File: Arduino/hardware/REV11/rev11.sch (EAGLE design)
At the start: 30 parts, among them IC2 ATMEGA168-AU, Q1 32768Hz

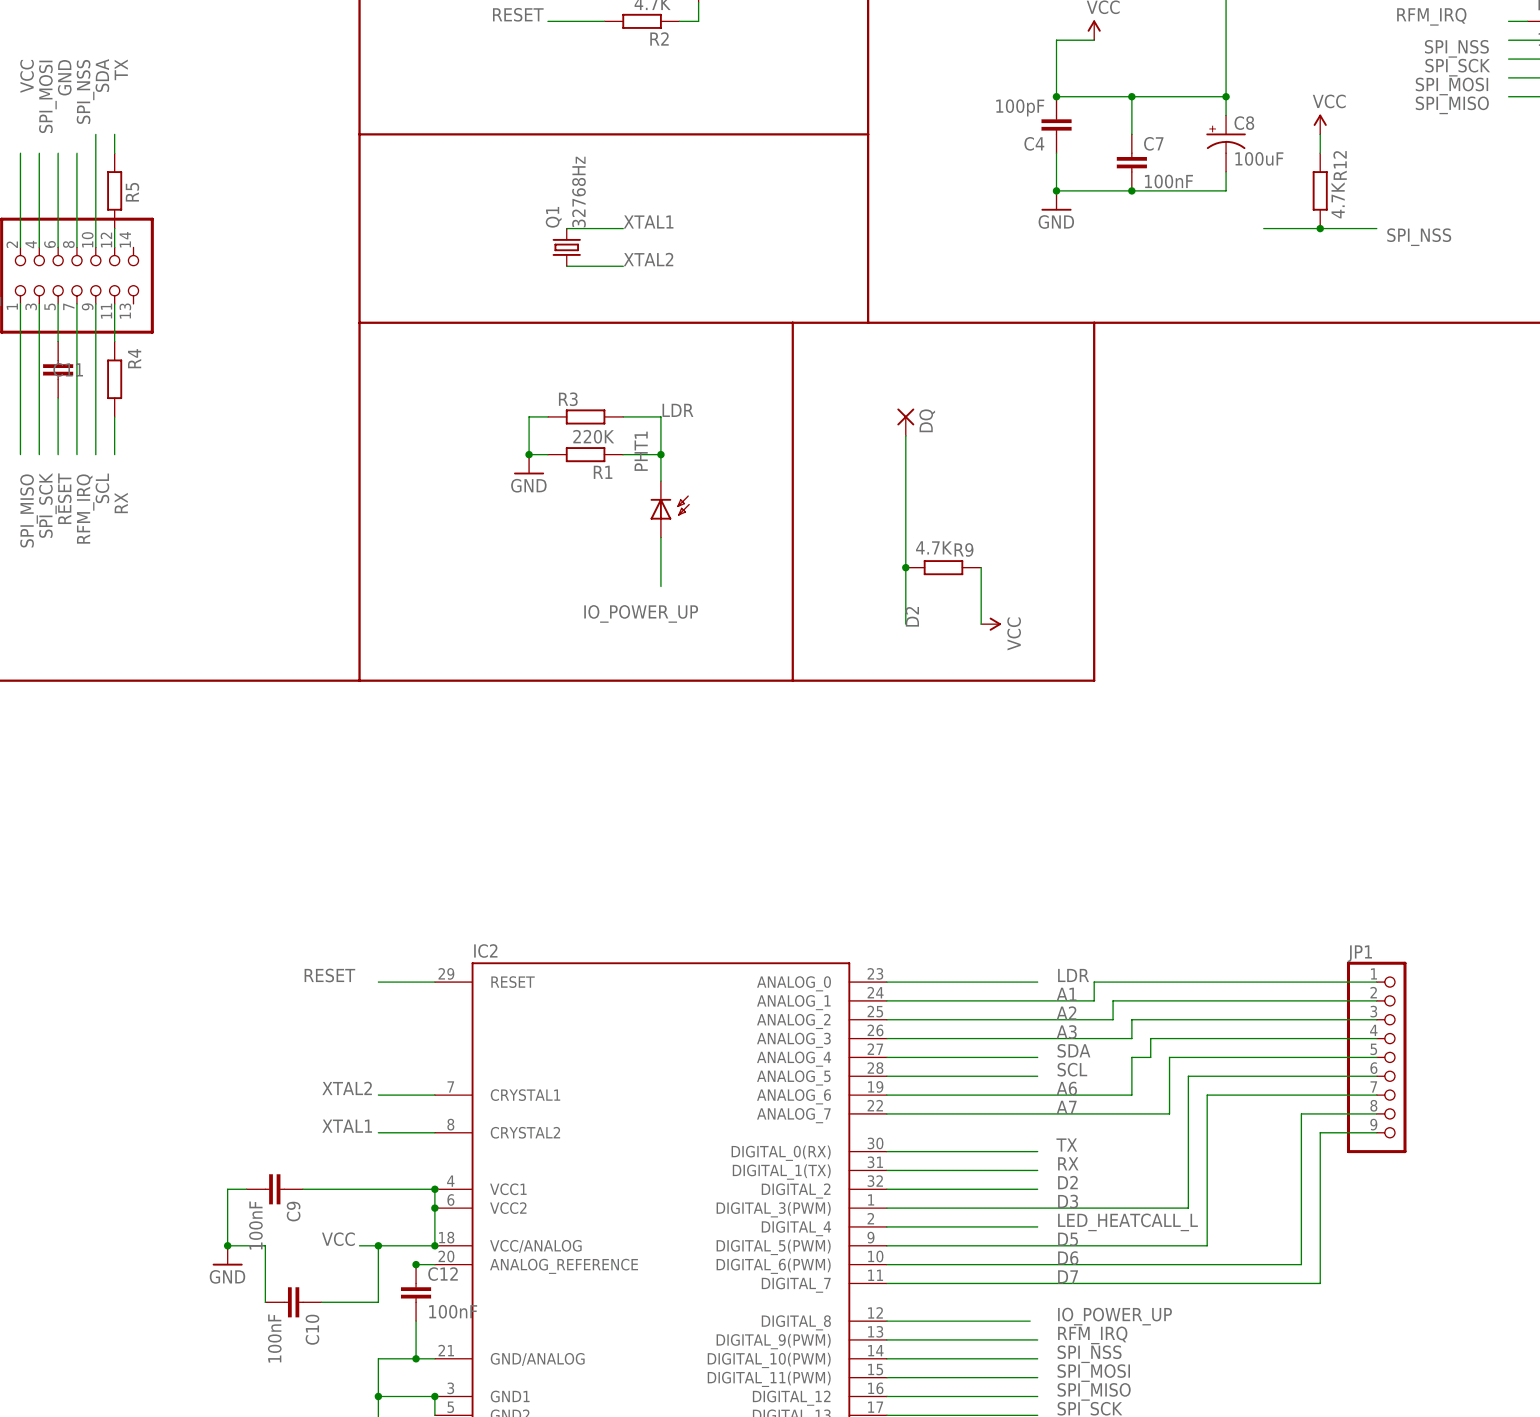
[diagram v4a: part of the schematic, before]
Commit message: moved DQ/D2 to gpio connector and I2C ext
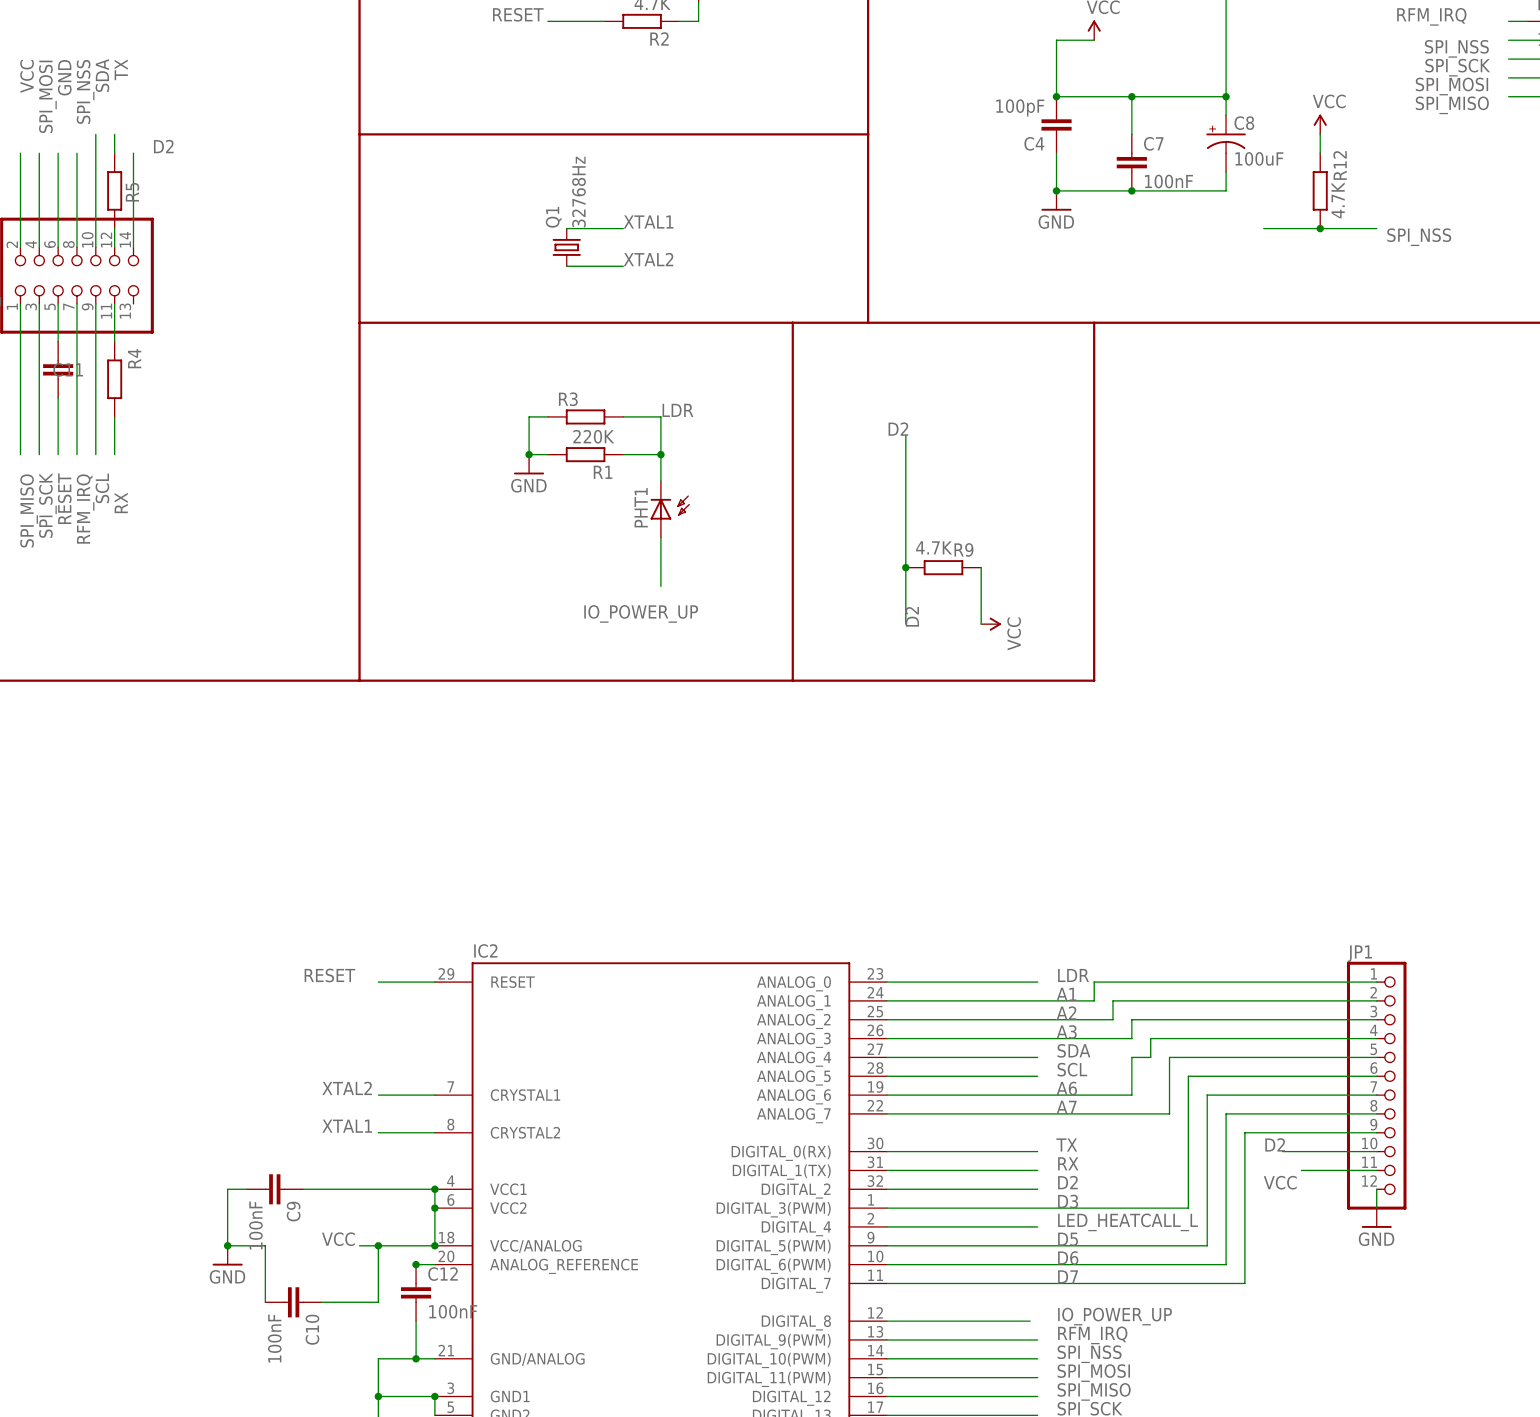
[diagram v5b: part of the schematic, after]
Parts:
- removed DQ: (no value), wirepad:2,15/1,0
- JP1: device pinhead:PINHD-1X9 -> pinhead:PINHD-1X12
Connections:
- net D2: now also JP1.10; no longer DQ.P
- net GND: now also JP1.12
- net VCC: now also JP1.11
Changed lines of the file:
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@@
 <part name="R9" library="resistor" deviceset="R-EU_" device="R0603" value="4.7K"/>
 <part name="P+1" library="SparkFun-Aesthetics" deviceset="VCC" device=""/>
-<part name="DQ" library="wirepad" deviceset="2,15/1,0" device=""/>
-<part name="JP1" library="pinhead" deviceset="PINHD-1X9" device=""/>
+<part name="JP1" library="pinhead" deviceset="PINHD-1X12" device=""/>
 <part name="PHT1" library="opto-trans-siemens" deviceset="BPX65" device=""/>
+<part name="GND2" library="SparkFun-Aesthetics" deviceset="GND" device=""/>
 </parts>
 <sheets>
@@
 </instance>
 <instance part="P+1" gate="G$1" x="241.3" y="167.64" rot="R270"/>
-<instance part="DQ" gate="1" x="231.14" y="195.58" rot="R270"/>
-<instance part="JP1" gate="A" x="297.18" y="109.22"/>
+<instance part="JP1" gate="G$1" x="297.18" y="106.68"/>
 <instance part="PHT1" gate="1" x="198.12" y="181.864" smashed="yes" rot="R180">
-<attribute name="NAME" x="194.564" y="193.802" size="1.778" layer="95" rot="R270"/>
-</instance>
+<attribute name="NAME" x="194.564" y="186.182" size="1.778" layer="95" rot="R270"/>
+</instance>
+<instance part="GND2" gate="1" x="294.64" y="86.36"/>
 </instances>
 <busses>
@@
 <wire x1="241.3" y1="167.64" x2="241.3" y2="175.26" width="0.1524" layer="91"/>
 </segment>
+<segment>
+<wire x1="294.64" y1="93.98" x2="284.48" y2="93.98" width="0.1524" layer="91"/>
+<label x="279.4" y="91.44" size="1.778" layer="95"/>
+<pinref part="JP1" gate="G$1" pin="11"/>
+</segment>
 </net>
 <net name="GND" class="1">
@@
 <junction x="180.34" y="190.5"/>
 </segment>
+<segment>
+<pinref part="JP1" gate="G$1" pin="12"/>
+<pinref part="GND2" gate="1" pin="GND"/>
+<wire x1="294.64" y1="88.9" x2="294.64" y2="91.44" width="0.1524" layer="91"/>
+</segment>
 </net>
 <net name="D6" class="0">
 <segment>
-<wire x1="228.6" y1="81.28" x2="284.48" y2="81.28" width="0.1524" layer="91"/>
-<wire x1="284.48" y1="81.28" x2="284.48" y2="101.6" width="0.1524" layer="91"/>
-<wire x1="284.48" y1="101.6" x2="294.64" y2="101.6" width="0.1524" layer="91"/>
+<wire x1="228.6" y1="81.28" x2="274.32" y2="81.28" width="0.1524" layer="91"/>
+<wire x1="274.32" y1="81.28" x2="274.32" y2="101.6" width="0.1524" layer="91"/>
+<wire x1="274.32" y1="101.6" x2="294.64" y2="101.6" width="0.1524" layer="91"/>
 <pinref part="IC2" gate="1" pin="DIGITAL_6(PWM)"/>
 <label x="251.46" y="81.28" size="1.778" layer="95"/>
-<pinref part="JP1" gate="A" pin="8"/>
+<pinref part="JP1" gate="G$1" pin="8"/>
 </segment>
 </net>
@@
 <pinref part="IC2" gate="1" pin="ANALOG_2"/>
 <label x="251.46" y="114.3" size="1.778" layer="95"/>
-<pinref part="JP1" gate="A" pin="2"/>
+<pinref part="JP1" gate="G$1" pin="2"/>
 </segment>
 </net>
@@
 <pinref part="IC2" gate="1" pin="DIGITAL_5(PWM)"/>
 <label x="251.46" y="83.82" size="1.778" layer="95"/>
-<pinref part="JP1" gate="A" pin="7"/>
+<pinref part="JP1" gate="G$1" pin="7"/>
 </segment>
 </net>
 <net name="D7" class="0">
 <segment>
-<wire x1="228.6" y1="78.74" x2="287.02" y2="78.74" width="0.1524" layer="91"/>
-<wire x1="287.02" y1="78.74" x2="287.02" y2="99.06" width="0.1524" layer="91"/>
-<wire x1="287.02" y1="99.06" x2="294.64" y2="99.06" width="0.1524" layer="91"/>
+<wire x1="228.6" y1="78.74" x2="276.86" y2="78.74" width="0.1524" layer="91"/>
+<wire x1="276.86" y1="78.74" x2="276.86" y2="99.06" width="0.1524" layer="91"/>
+<wire x1="276.86" y1="99.06" x2="294.64" y2="99.06" width="0.1524" layer="91"/>
 <pinref part="IC2" gate="1" pin="DIGITAL_7"/>
 <label x="251.46" y="78.74" size="1.778" layer="95"/>
-<pinref part="JP1" gate="A" pin="9"/>
+<pinref part="JP1" gate="G$1" pin="9"/>
 </segment>
 </net>
@@
 <junction x="231.14" y="175.26"/>
 <label x="231.14" y="170.18" size="1.778" layer="95" rot="R270"/>
-<pinref part="DQ" gate="1" pin="P"/>
+<label x="228.6" y="193.04" size="1.778" layer="95"/>
+</segment>
+<segment>
+<wire x1="281.94" y1="96.52" x2="294.64" y2="96.52" width="0.1524" layer="91"/>
+<label x="279.4" y="96.52" size="1.778" layer="95"/>
+<pinref part="JP1" gate="G$1" pin="10"/>
+</segment>
+<segment>
+<wire x1="127" y1="231.14" x2="127" y2="218.44" width="0.1524" layer="91"/>
+<label x="129.54" y="231.14" size="1.778" layer="95"/>
 </segment>
 </net>
@@
 <wire x1="256.54" y1="119.38" x2="294.64" y2="119.38" width="0.1524" layer="91"/>
 <label x="251.46" y="116.84" size="1.778" layer="95"/>
-<pinref part="JP1" gate="A" pin="1"/>
+<pinref part="JP1" gate="G$1" pin="1"/>
 </segment>
 </net>
@@
 <wire x1="269.24" y1="106.68" x2="294.64" y2="106.68" width="0.1524" layer="91"/>
 <label x="251.46" y="88.9" size="1.778" layer="95"/>
-<pinref part="JP1" gate="A" pin="6"/>
+<pinref part="JP1" gate="G$1" pin="6"/>
 </segment>
 </net>
@@
 <wire x1="261.62" y1="114.3" x2="294.64" y2="114.3" width="0.1524" layer="91"/>
 <label x="251.46" y="111.76" size="1.778" layer="95"/>
-<pinref part="JP1" gate="A" pin="3"/>
+<pinref part="JP1" gate="G$1" pin="3"/>
 </segment>
 </net>
@@
 <wire x1="264.16" y1="111.76" x2="294.64" y2="111.76" width="0.1524" layer="91"/>
 <label x="251.46" y="104.14" size="1.778" layer="95"/>
-<pinref part="JP1" gate="A" pin="4"/>
+<pinref part="JP1" gate="G$1" pin="4"/>
 </segment>
 </net>
@@
 <wire x1="266.7" y1="109.22" x2="294.64" y2="109.22" width="0.1524" layer="91"/>
 <label x="251.46" y="101.6" size="1.778" layer="95"/>
-<pinref part="JP1" gate="A" pin="5"/>
-</segment>
-</net>
+<pinref part="JP1" gate="G$1" pin="5"/>
+</segment>
+</net>

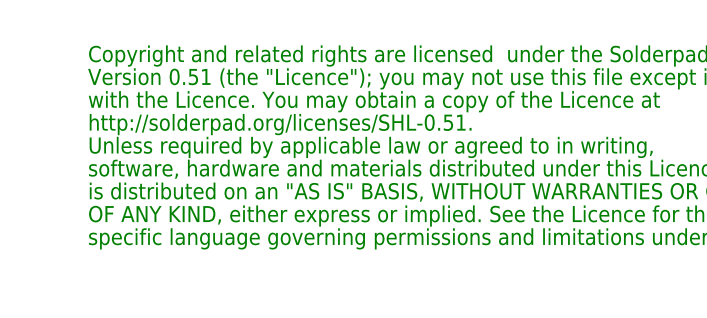
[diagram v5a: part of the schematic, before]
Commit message: corrected antenna and added copyright
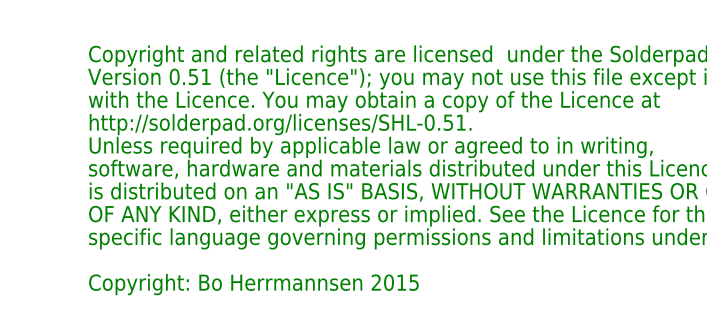
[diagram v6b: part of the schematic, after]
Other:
- note added: "Copyright: Bo Herrmannsen 2015"
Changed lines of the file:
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@@
 <wire x1="157.48" y1="160.02" x2="256.54" y2="160.02" width="0.3048" layer="94"/>
 <wire x1="256.54" y1="208.28" x2="256.54" y2="160.02" width="0.3048" layer="94"/>
+<text x="7.62" y="2.54" size="1.778" layer="91">Copyright: Bo Herrmannsen 2015</text>
 </plain>
 <instances>

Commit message: updates to both rev10 and rev11
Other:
- moved on the sheet: +, -
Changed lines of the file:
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@@
 <?xml version="1.0" encoding="utf-8"?>
 <!DOCTYPE eagle SYSTEM "eagle.dtd">
-<eagle version="7.3.0">
+<eagle version="7.4.0">
 <drawing>
 <settings>
@@
 <part name="ANT" library="wirepad" deviceset="SMD2" device=""/>
 <part name="P+5" library="SparkFun-Aesthetics" deviceset="VCC" device=""/>
-<part name="+" library="wirepad" deviceset="2,15/1,0" device=""/>
-<part name="-" library="wirepad" deviceset="2,15/1,0" device=""/>
 <part name="GND7" library="SparkFun-Aesthetics" deviceset="GND" device=""/>
 <part name="R1" library="resistor" deviceset="R-EU_" device="R0603" value="220K"/>
@@
 <part name="PHT1" library="opto-trans-siemens" deviceset="BPX65" device=""/>
 <part name="GND2" library="SparkFun-Aesthetics" deviceset="GND" device=""/>
+<part name="-" library="wirepad" deviceset="2,15/1,0" device=""/>
+<part name="+" library="wirepad" deviceset="2,15/1,0" device=""/>
 </parts>
 <sheets>
@@
 <instance part="ANT" gate="1" x="370.84" y="254" rot="R180"/>
 <instance part="P+5" gate="G$1" x="25.4" y="243.84"/>
-<instance part="+" gate="1" x="12.7" y="238.76"/>
-<instance part="-" gate="1" x="12.7" y="233.68"/>
 <instance part="GND7" gate="1" x="180.34" y="187.96"/>
 <instance part="R1" gate="G$1" x="187.96" y="190.5" rot="R180"/>
@@
 </instance>
 <instance part="GND2" gate="1" x="294.64" y="86.36"/>
+<instance part="-" gate="1" x="7.62" y="231.14"/>
+<instance part="+" gate="1" x="7.62" y="238.76"/>
 </instances>
 <busses>
@@
 <segment>
 <wire x1="25.4" y1="243.84" x2="25.4" y2="238.76" width="0.1524" layer="91"/>
-<wire x1="25.4" y1="238.76" x2="15.24" y2="238.76" width="0.1524" layer="91"/>
+<wire x1="25.4" y1="238.76" x2="10.16" y2="238.76" width="0.1524" layer="91"/>
 <pinref part="P+5" gate="G$1" pin="VCC"/>
 <pinref part="+" gate="1" pin="P"/>
@@
 <segment>
 <pinref part="GND1" gate="1" pin="GND"/>
-<wire x1="15.24" y1="231.14" x2="15.24" y2="233.68" width="0.1524" layer="91"/>
+<wire x1="10.16" y1="231.14" x2="15.24" y2="231.14" width="0.1524" layer="91"/>
 <pinref part="-" gate="1" pin="P"/>
 </segment>

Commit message: updates to rev11
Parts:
- removed R3: (no value), resistor:R-EU_0309/V
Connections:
- net GND: no longer R3.1
- net LDR: no longer R3.2
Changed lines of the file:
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@@
 <part name="GND7" library="SparkFun-Aesthetics" deviceset="GND" device=""/>
 <part name="R1" library="resistor" deviceset="R-EU_" device="R0603" value="220K"/>
-<part name="R3" library="resistor" deviceset="R-EU_" device="0309/V"/>
 <part name="R9" library="resistor" deviceset="R-EU_" device="R0603" value="4.7K"/>
 <part name="P+1" library="SparkFun-Aesthetics" deviceset="VCC" device=""/>
@@
 <instance part="GND7" gate="1" x="180.34" y="187.96"/>
 <instance part="R1" gate="G$1" x="187.96" y="190.5" rot="R180"/>
-<instance part="R3" gate="G$1" x="187.96" y="195.58"/>
 <instance part="R9" gate="G$1" x="236.22" y="175.26" smashed="yes">
 <attribute name="NAME" x="237.49" y="176.7586" size="1.778" layer="95"/>
@@
 <wire x1="180.34" y1="190.5" x2="182.88" y2="190.5" width="0.1524" layer="91"/>
 <pinref part="R1" gate="G$1" pin="2"/>
-<pinref part="R3" gate="G$1" pin="1"/>
-<wire x1="182.88" y1="195.58" x2="180.34" y2="195.58" width="0.1524" layer="91"/>
-<wire x1="180.34" y1="195.58" x2="180.34" y2="190.5" width="0.1524" layer="91"/>
-<junction x="180.34" y="190.5"/>
 </segment>
 <segment>
@@
 <net name="LDR" class="0">
 <segment>
-<wire x1="198.12" y1="195.58" x2="198.12" y2="190.5" width="0.1524" layer="91"/>
 <pinref part="R1" gate="G$1" pin="1"/>
 <wire x1="198.12" y1="190.5" x2="198.12" y2="186.944" width="0.1524" layer="91"/>
 <wire x1="193.04" y1="190.5" x2="198.12" y2="190.5" width="0.1524" layer="91"/>
-<junction x="198.12" y="190.5"/>
-<pinref part="R3" gate="G$1" pin="2"/>
-<wire x1="198.12" y1="195.58" x2="193.04" y2="195.58" width="0.1524" layer="91"/>
-<label x="198.12" y="195.58" size="1.778" layer="95"/>
+<label x="198.12" y="190.5" size="1.778" layer="95"/>
 <pinref part="PHT1" gate="1" pin="C"/>
 </segment>
